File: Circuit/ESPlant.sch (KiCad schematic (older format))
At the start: 19 parts, among them IC1 UFQFPN48, P1 SOLAR, P2 USB_5PIN_SHELL, SW1 RESET, SW2 PRGM, U1 ESP-12E

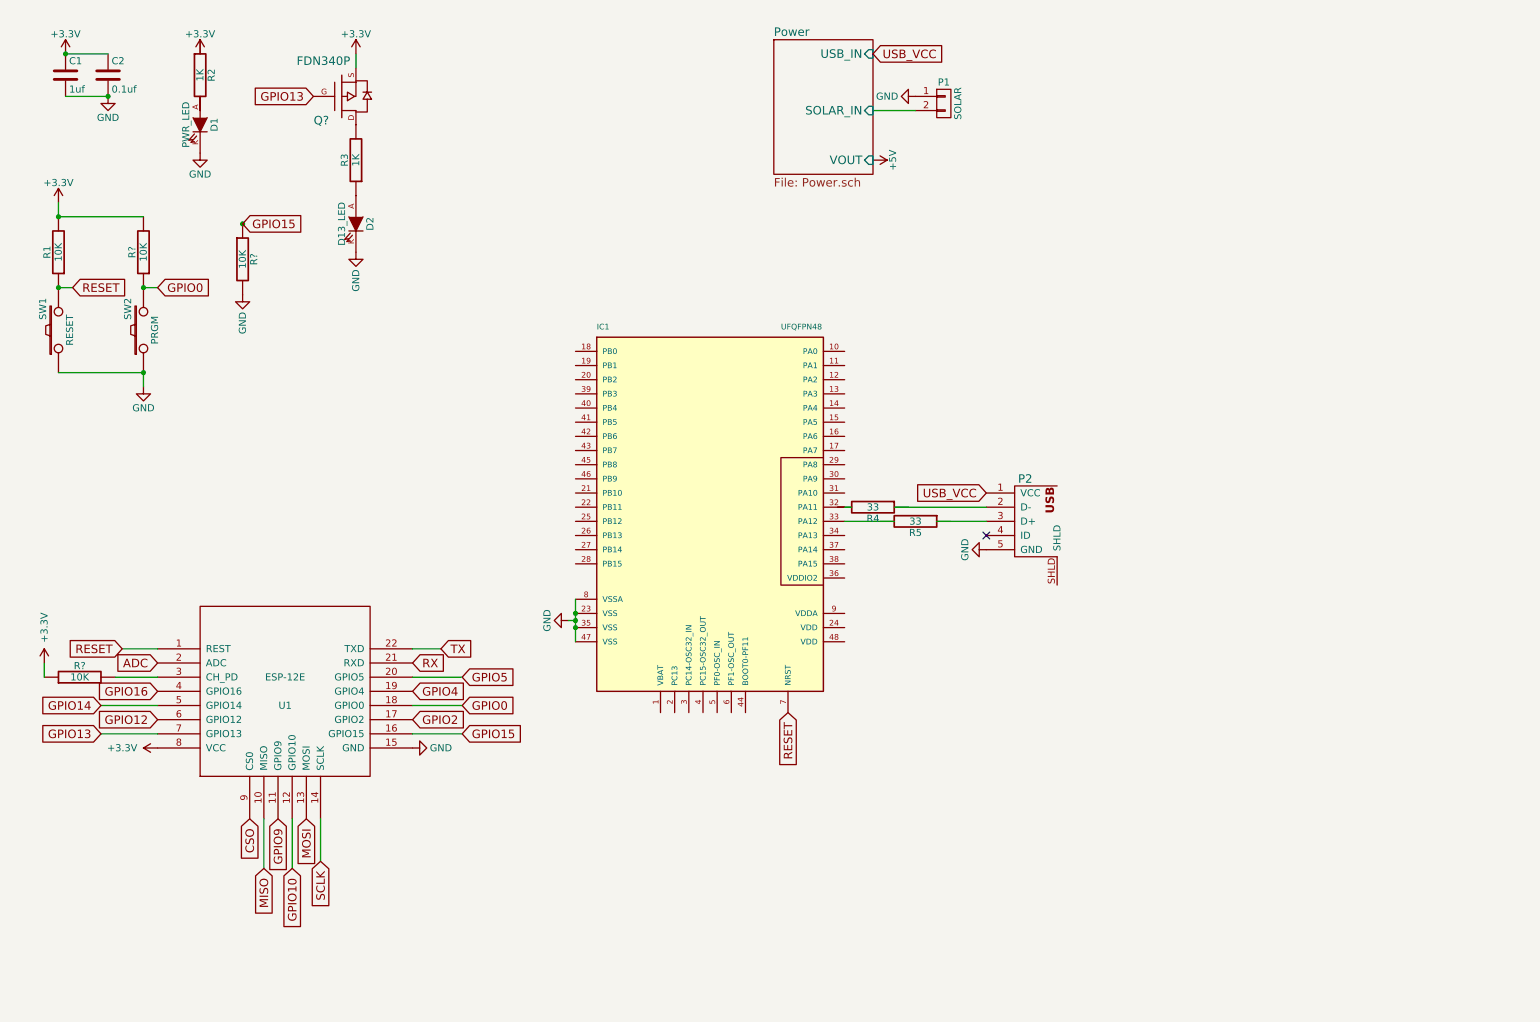
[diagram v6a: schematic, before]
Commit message: Flesh out schematic sensor elements, etc.
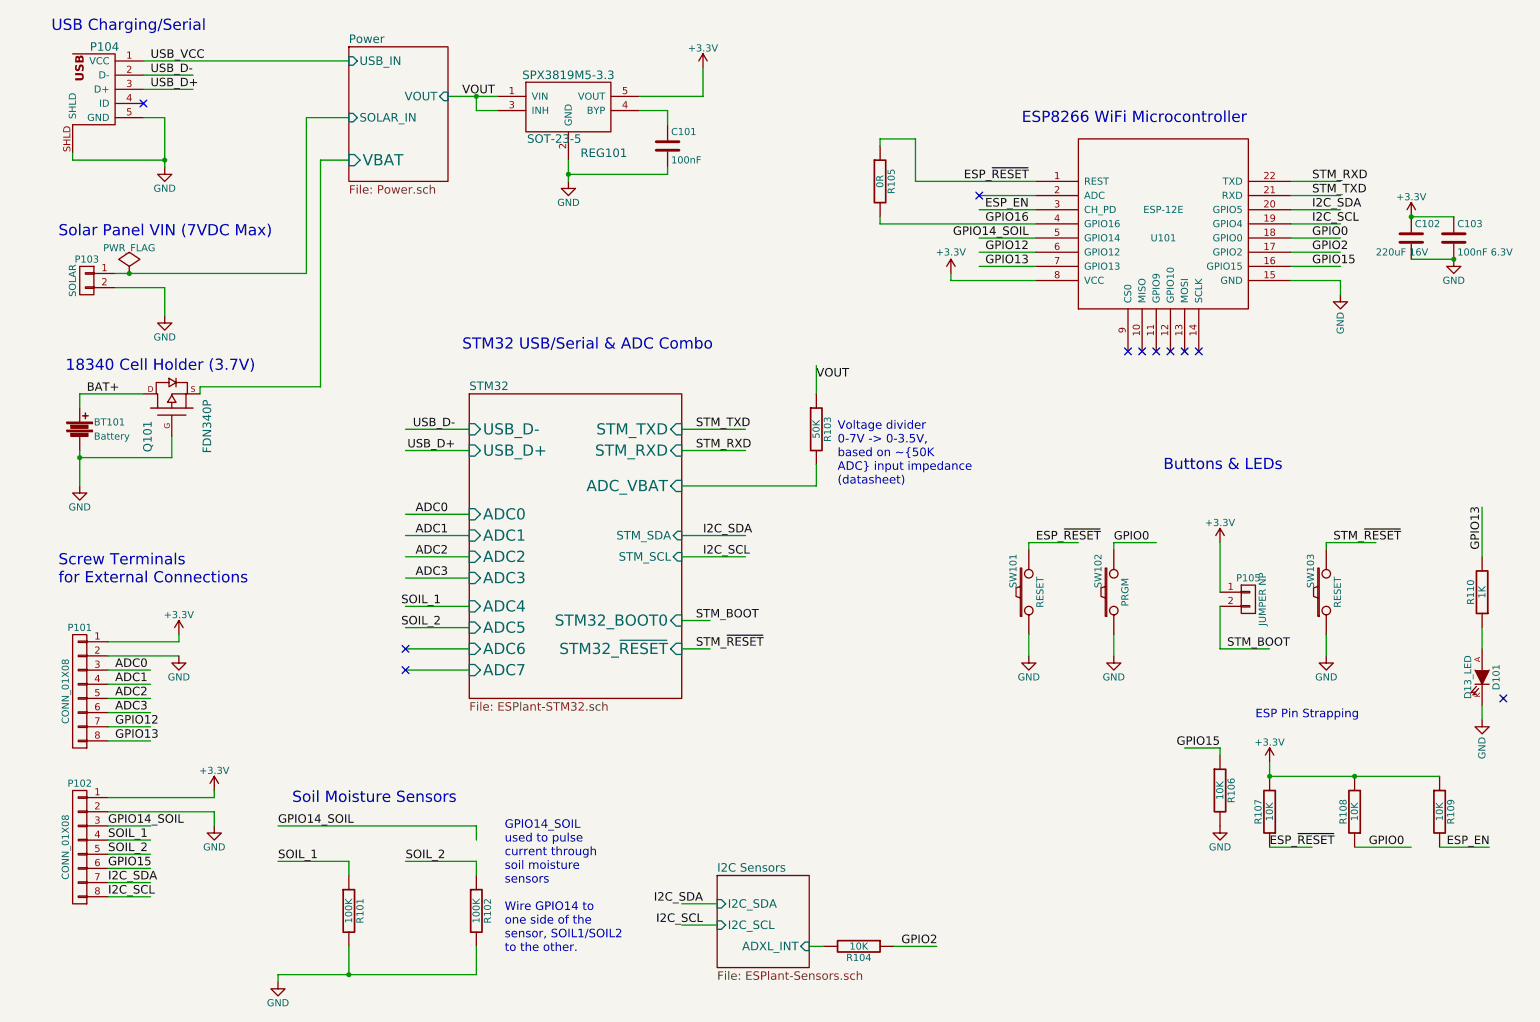
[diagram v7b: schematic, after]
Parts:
- removed D1: PWR_LED, symbol LED
- removed IC1: UFQFPN48, symbol UFQFPN48
- removed Q?: FDN340P, symbol MOSFET_P
- removed R2: 1K, symbol R
- removed R4, R5: 33, symbol R
- removed R?: 10K, symbol R
- removed SW1: RESET, symbol SW_PUSH
- removed SW2: PRGM, symbol SW_PUSH
- added BT101: Battery, symbol Battery
- added C101: 100nF, symbol C
- added P101, P102: CONN_01X08, symbol CONN_01X08
- added P105: JUMPER NP, symbol CONN_01X02
- added Q101: FDN340P, symbol MOSFET_P
- added R101, R102: 100K, symbol R
- added R103: 50K, symbol R
- added R104, R109: 10K, symbol R
- added R105: 0R, symbol R
- added REG101: SPX3819M5-3.3, SOT-23-5, symbol LD3985M
- added SW101, SW103: RESET, symbol SW_PUSH
- added SW102: PRGM, symbol SW_PUSH
- C102: renamed from C1; value 1uf -> 220uF 16V
- C103: renamed from C2; value 0.1uf -> 100nF 6.3V
- gave numbers to parts that had none: 2
- renumbered D2 to D101, P1 to P103, P2 to P104, R1 to R107, R3 to R110, U1 to U101
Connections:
- net labels added: ADC0, ADC1, ADC2, ADC3, BAT+, ESP_EN, ESP_~RESET, GPIO14_SOIL, I2C_SCL, I2C_SDA, SOIL_1, SOIL_2, STM_BOOT, STM_RXD, STM_TXD, STM_~RESET, USB_D+, USB_D-, VOUT
- net labels removed: +5V, ADC, CSO, GPIO10, GPIO14, GPIO4, GPIO5, GPIO9, MISO, MOSI, RESET, RX, SCLK, TX
- wire segments 31 -> 130
- no-connect marks 1 -> 11
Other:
- note added: "18340 Cell Holder (3.7V)\n"
- note added: "Buttons & LEDs"
- note added: "ESP Pin Strapping"
- note added: "ESP8266 WiFi Microcontroller"
- note added: "GPIO14_SOIL\nused to pulse\ncurrent through\nsoil moisture\nsensors\n\nWire GPIO14 to\none side of the\nsensor, SOIL1/SOIL2\nto the other."
- note added: "STM32 USB/Serial & ADC Combo"
- note added: "Screw Terminals\nfor External Connections"
- note added: "Soil Moisture Sensors\n"
- note added: "Solar Panel VIN (7VDC Max)"
- note added: "USB Charging/Serial"
- note added: "Voltage divider\n0-7V -> 0-3.5V,\nbased on ~50K\nADC input impedance\n(datasheet)"
- moved on the sheet: C102, C103, D101, P103, P104, R106, R107, R108, R110, U101

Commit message: Downgrade STM32 to cute little TSSOP20 STM32F042F6
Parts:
- removed P105: JUMPER NP, symbol CONN_01X02
- added C102: 100nF 6.3V, symbol C
- added C103: 10uF 16V, symbol C
- added C104: 100nF, symbol C
- added P105: CONN_01X05, symbol CONN_01X05
- added R101: 10K DNP, symbol R
- added R107: 47K 1%, symbol R
- added U101: STM32F042F, symbol STM32F042F
- R106: renamed from R103; value 50K -> 56K 1%
- REG101: symbol LD3985M -> LD3985M-RESCUE-ESPlant
- renumbered C102 to C105, C103 to C106, R101 to R102, R102 to R103, R106 to R108, R107 to R109, R108 to R110, R109 to R111, R110 to R112, U101 to U102
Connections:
- net labels added: STM_SWCLK, STM_SWDIO
- wire segments 130 -> 151
- no-connect marks 11 -> 9
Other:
- note added: "Input voltage\nmonitor via divider\n0-7V -> 0-3.2V,\n"
- note added: "Pulldown is NP\nas BOOT0 pin\ncan be disabled\nin flash config sector."
- note added: "STM32 SWD\nProgramming\nHeader (Optional)"
- note removed: "Voltage divider\n0-7V -> 0-3.5V,\nbased on ~50K\nADC input impedance\n(datasheet)"
- moved on the sheet: R106, SW101, SW102, SW103
